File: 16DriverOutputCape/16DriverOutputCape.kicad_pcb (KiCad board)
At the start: 2 copper layers, 54.6 x 111.8 mm, 16 parts, among them P1 0 1 2, P2 C A0 A1 A2 A3 A4 A5 A6 A7, P3 C B0 B1 B2 B3 B4 B5 B6 B7, P8 BeagleBone_Black_Header, P9 BeagleBone_Black_Header, U1 MCP23017, U2 TBD62X83A, U3 TBD62X83A

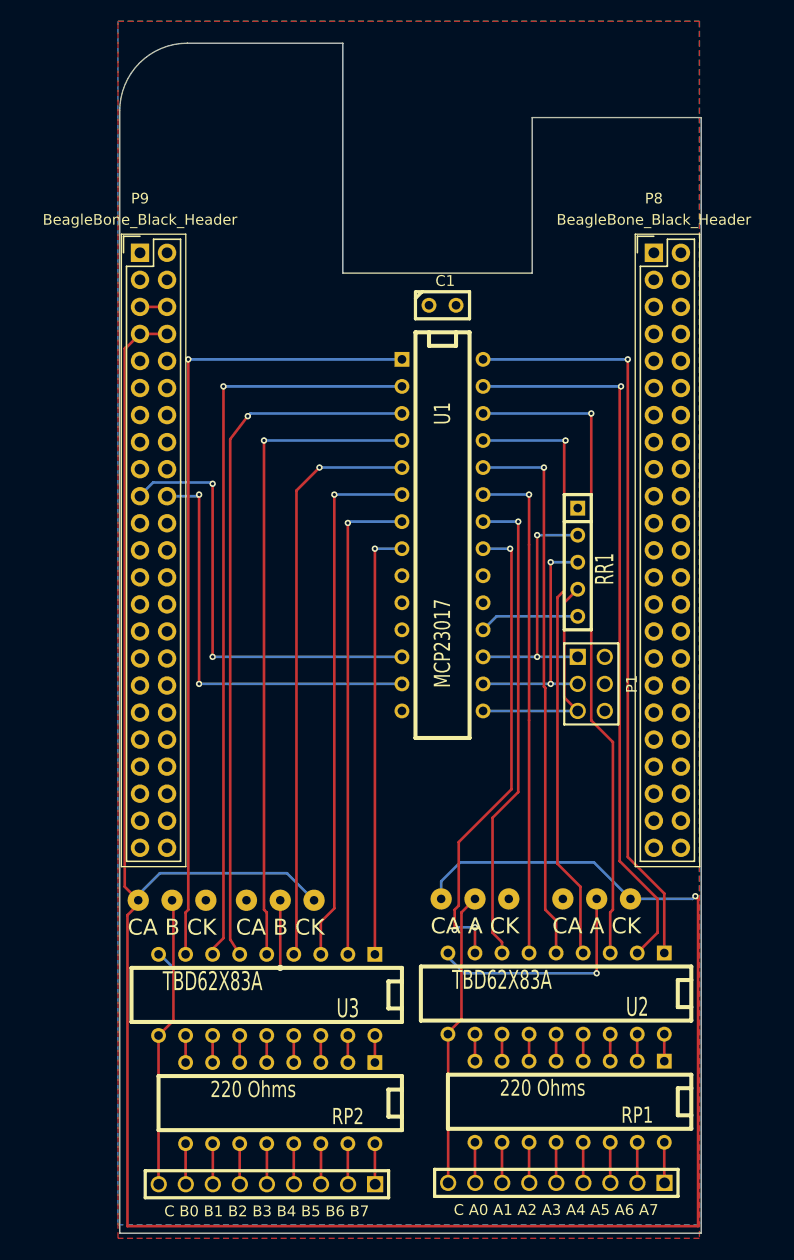
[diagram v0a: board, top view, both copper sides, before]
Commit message: Update 16DriverOutputCape to use 12V for the LEDs.
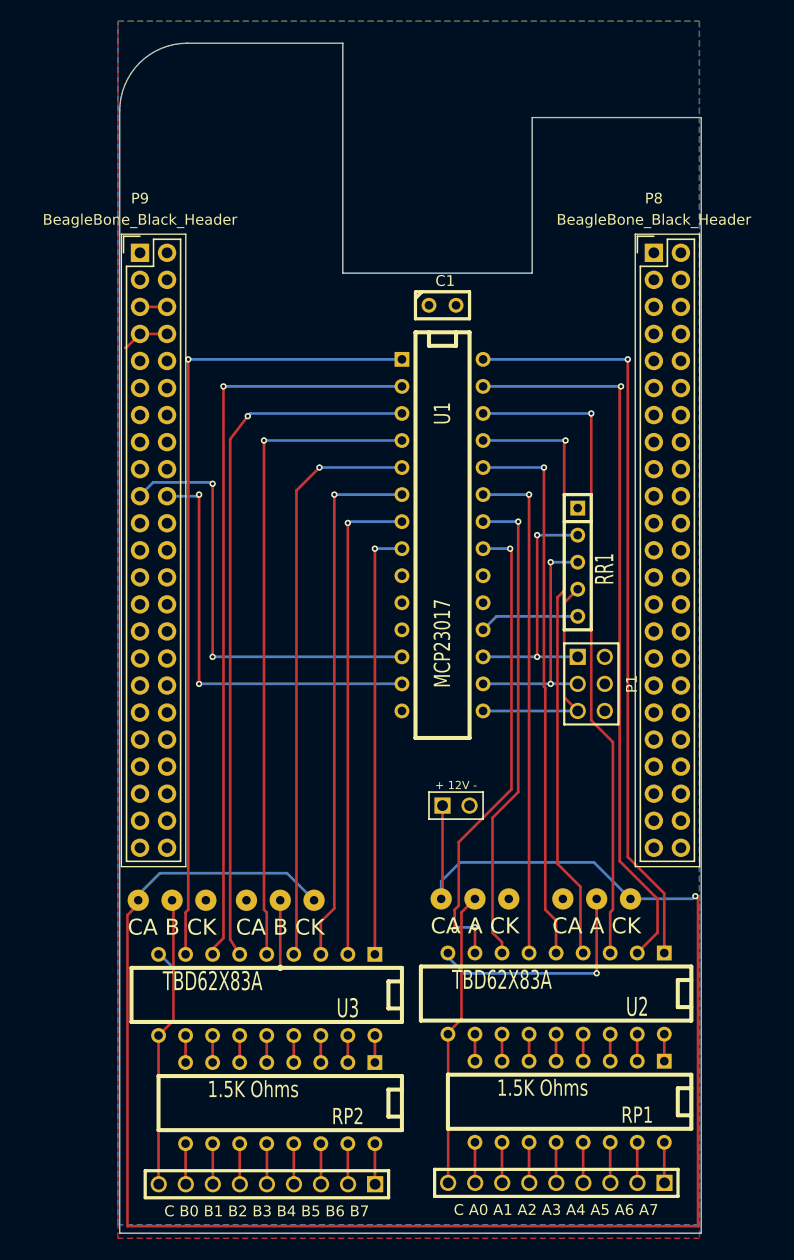
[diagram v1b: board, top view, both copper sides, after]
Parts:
- added T1: + 12V -, ScrewTerm2.54-2, F.Cu at (146.1, 114.3)
- RP1, RP2: value 220 Ohms -> 1.5K Ohms
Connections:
- JP1 pad 1: SYS_5V -> +12V
- JP2 pad 3: SYS_5V -> +12V
- JP3 pad 1: SYS_5V -> +12V
- JP4 pad 3: SYS_5V -> +12V
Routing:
- net SYS_5V: track 219.4 -> 4.54 mm, vias 1 -> 0
- net +12V: track 0.00 -> 171.2 mm, vias 0 -> 1

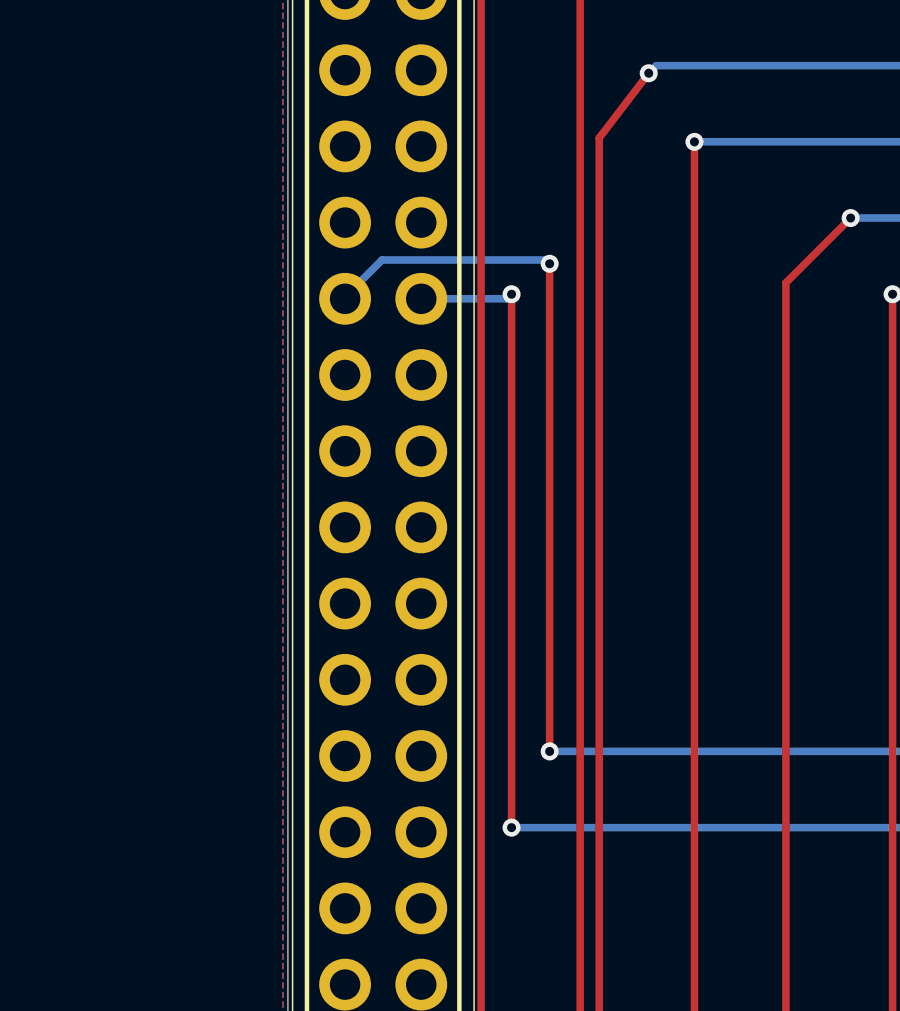
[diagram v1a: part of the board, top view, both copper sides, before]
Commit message: Change expander I2C buss from I2C2 to I2C1.
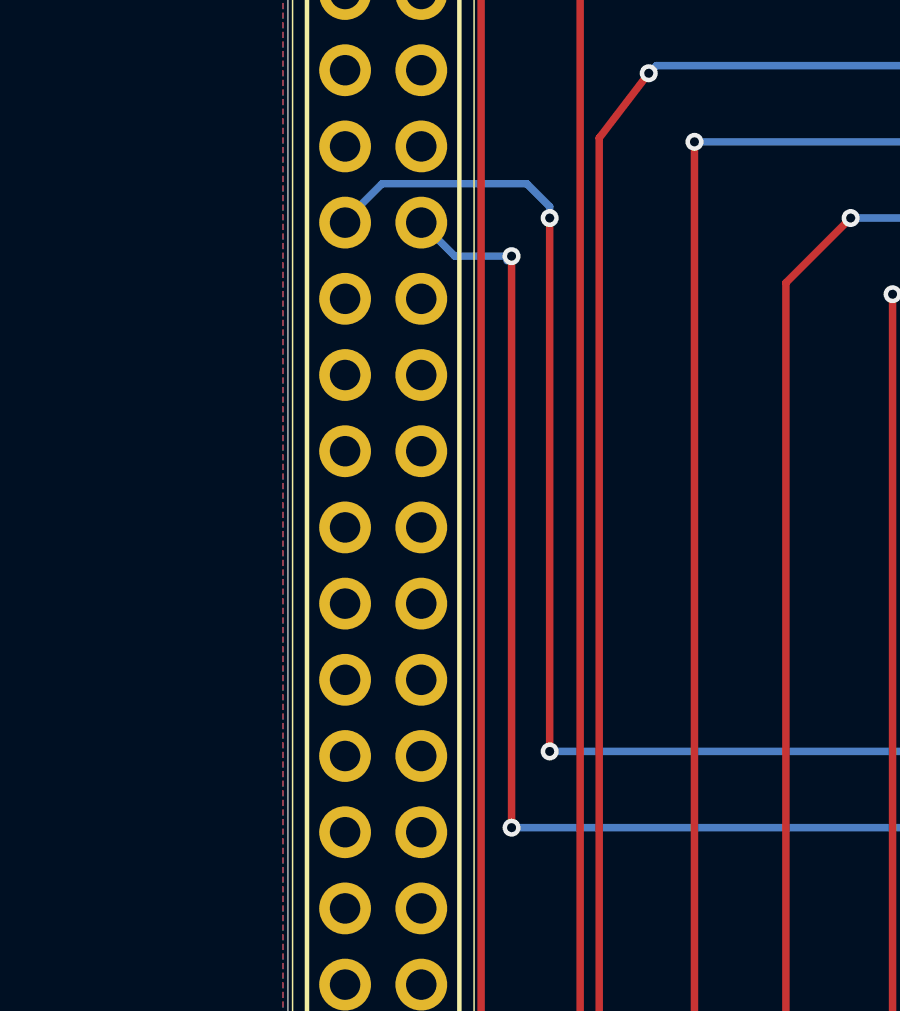
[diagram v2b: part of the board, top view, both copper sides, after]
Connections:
- P9 pad 17: (no net) -> /Drivers/SCL
- P9 pad 18: (no net) -> /Drivers/SDA
- P9 pad 19: /Drivers/SCL -> (no net)
- P9 pad 20: /Drivers/SDA -> (no net)
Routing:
- net /Drivers/SCL: track 41.5 -> 43.7 mm
- net /Drivers/SDA: track 39.9 -> 41.8 mm

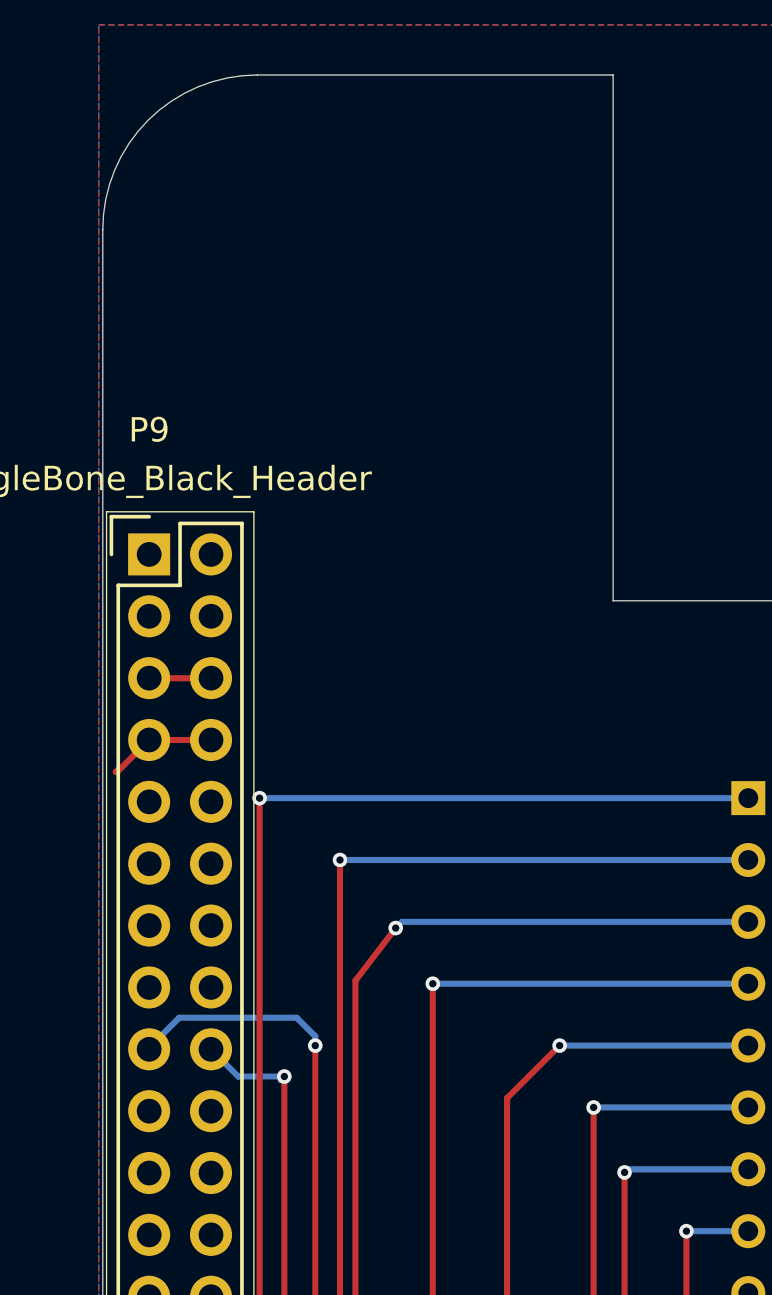
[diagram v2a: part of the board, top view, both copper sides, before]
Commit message: Add EEProm to 16DriverOutputCape.
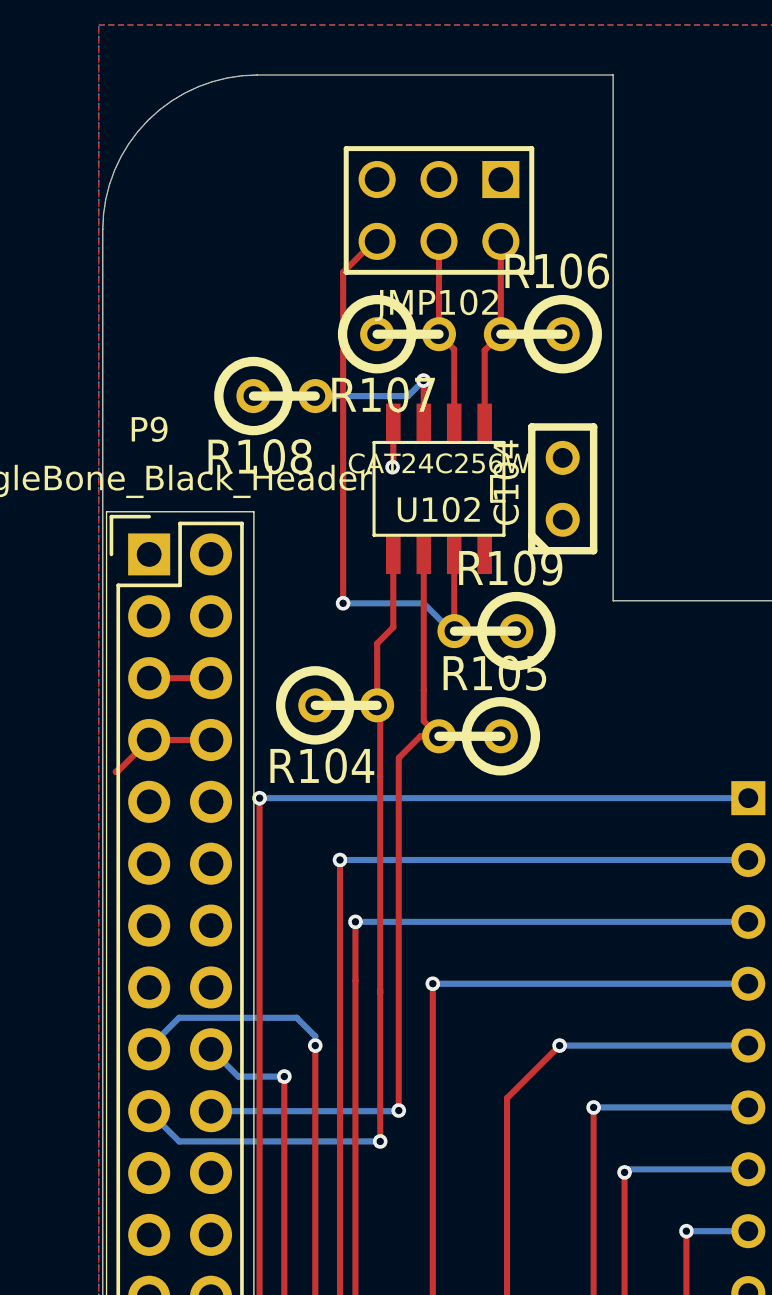
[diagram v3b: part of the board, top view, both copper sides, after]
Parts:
- added C104: .1 uf, C1, F.Cu at (133.3, 59.7)
- added JMP102: WP 1 0, pin_array_3x2, F.Cu at (128.3, 48.3)
- added R104: 5.6K Ohms, R1, F.Cu at (124.5, 68.6)
- added R105: 5.6K Ohms, R1, F.Cu at (129.5, 69.8)
- added R106: 4.75K Ohms, R1, F.Cu at (132.1, 53.3)
- added R107: 4.75K Ohms, R1, F.Cu at (127.0, 53.3)
- added R108: 4.75K Ohms, R1, F.Cu at (121.9, 55.9)
- added R109: 10K Ohms, R1, F.Cu at (130.2, 65.5)
- added U102: CAT24C256W, SOIC-8_N, F.Cu at (128.3, 59.7)
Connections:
- P9 pad 19: (no net) -> /Cape EEProm/SDA2
- P9 pad 20: (no net) -> /Cape EEProm/SCL2
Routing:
- net /Cape EEProm/SDA2: track 0.00 -> 34.6 mm, vias 0 -> 1
- net /Cape EEProm/SCL2: track 0.00 -> 31.9 mm, vias 0 -> 1
- net N-0000086: track 0.00 -> 23.7 mm, vias 0 -> 1
- net N-0000085: track 0.00 -> 7.74 mm
- net N-0000084: track 0.00 -> 7.72 mm
- net N-0000083: track 0.00 -> 6.46 mm, vias 0 -> 1
- net GND: track 0.00 -> 1.82 mm, vias 0 -> 1
- net N-00000153: track 65.9 -> 67.2 mm

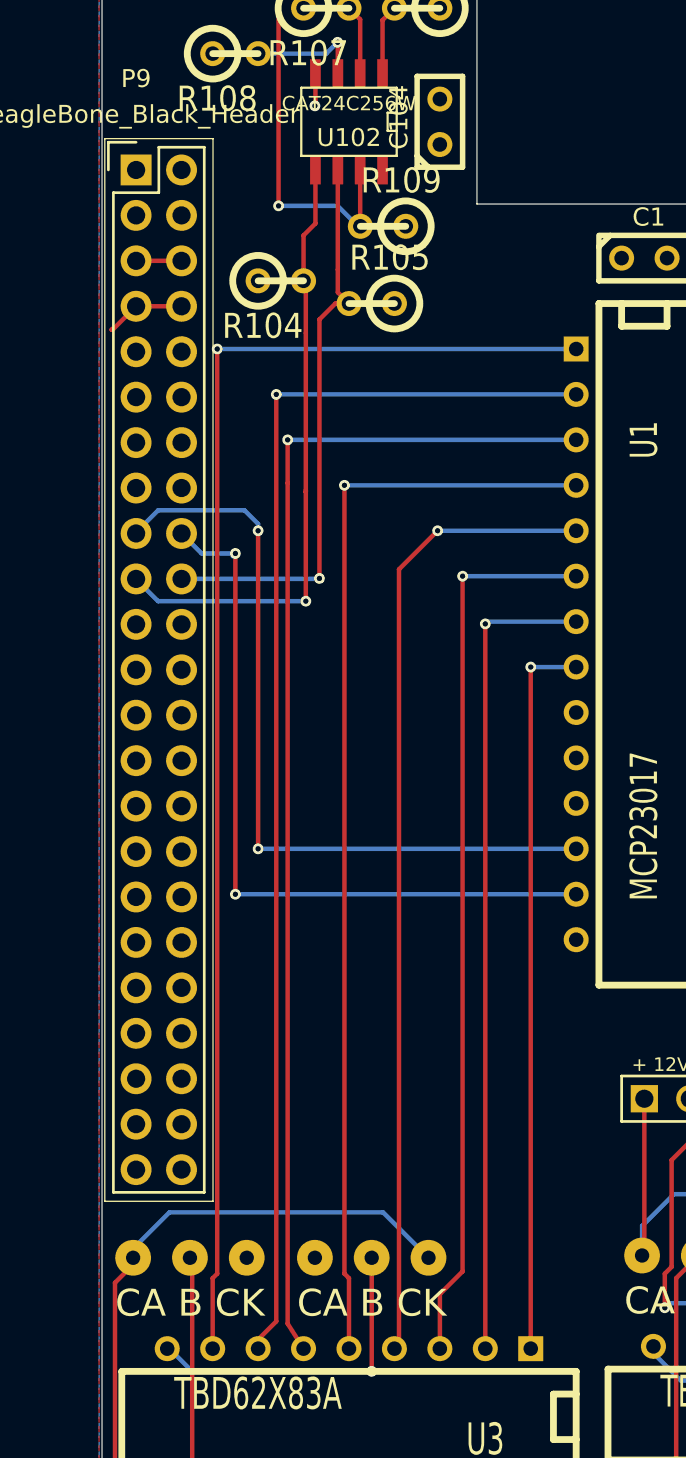
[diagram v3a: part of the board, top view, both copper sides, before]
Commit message: Add serial pass-through header to 16DriverOutputCape. Also fix swapped I2C lines.
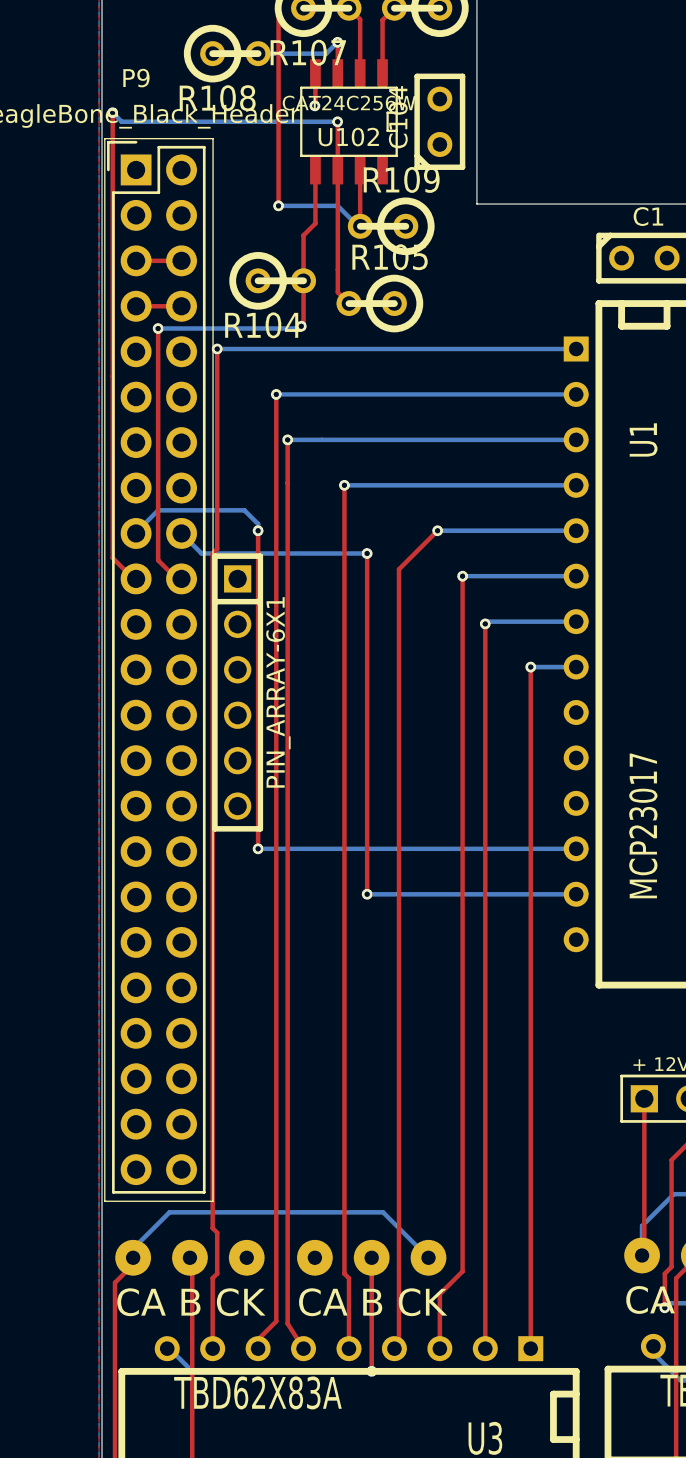
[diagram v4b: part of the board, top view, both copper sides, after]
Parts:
- added PIN_ARRAY-6X1: Val**, PIN_ARRAY-6X1, F.Cu at (122.0, 91.6)
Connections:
- P9 pad 19: /Cape EEProm/SDA2 -> /Cape EEProm/SCL2
- P9 pad 20: /Cape EEProm/SCL2 -> /Cape EEProm/SDA2
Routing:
- net /Cape EEProm/SCL2: track 31.9 -> 49.9 mm, vias 1 -> 2
- net /Cape EEProm/SDA2: track 34.6 -> 31.8 mm, vias 1 -> 2
- net SYS_5V: track 4.54 -> 2.54 mm
